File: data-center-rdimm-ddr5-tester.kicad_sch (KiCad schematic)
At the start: 2 parts

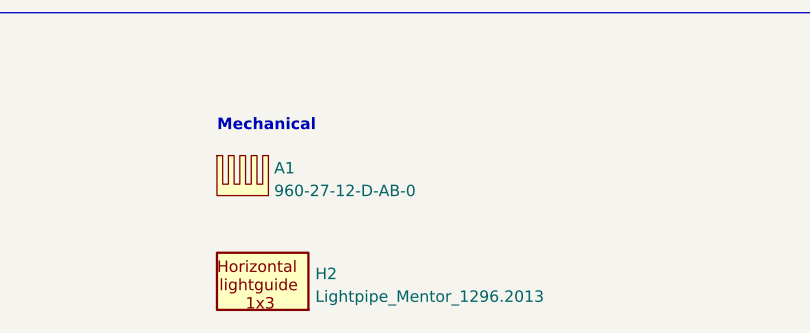
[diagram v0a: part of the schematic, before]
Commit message: [#67402] Connect low speed signals and interfaces to the HD banks. Optimize connection in bank 86
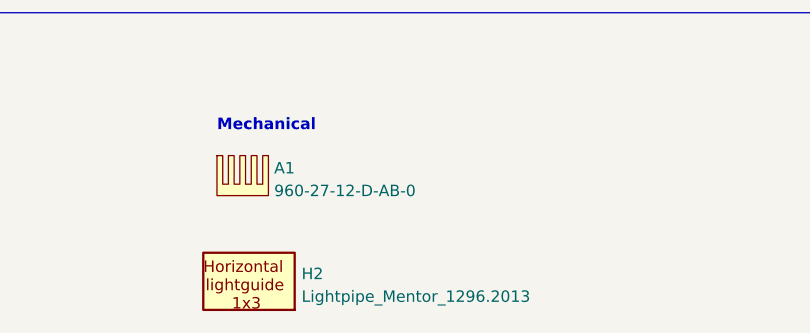
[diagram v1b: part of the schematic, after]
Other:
- moved on the sheet: H2
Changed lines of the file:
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@@
     )
   )
-  (symbol (lib_id "antmicroMechanicalParts:Lightpipe_Mentor_1296.2013") (at 259.08 276.86 0) (unit 1)
+  (symbol (lib_id "antmicroMechanicalParts:Lightpipe_Mentor_1296.2013") (at 257.556 276.86 0) (unit 1)
     (in_bom yes) (on_board yes) (dnp no) (fields_autoplaced)
-    (property "Reference" "H2" (at 264.922 275.3944 0)
+    (property "Reference" "H2" (at 263.398 275.3944 0)
       (effects (font (size 1.27 1.27) (thickness 0.15)) (justify left))
     )
-    (property "Value" "Lightpipe_Mentor_1296.2013" (at 264.922 277.9181 0)
+    (property "Value" "Lightpipe_Mentor_1296.2013" (at 263.398 277.9181 0)
       (effects (font (size 1.27 1.27) (thickness 0.15)) (justify left))
     )
-    (property "Footprint" "antmicro-footprints:Mech_Lightpipe_Mentor_1296.2013" (at 279.4 284.48 0)
+    (property "Footprint" "antmicro-footprints:Mech_Lightpipe_Mentor_1296.2013" (at 277.876 284.48 0)
       (effects (font (size 1.27 1.27) (thickness 0.15)) (justify left bottom) hide)
     )
-    (property "Datasheet" "https://docs.rs-online.com/e47b/0900766b813f6efb.pdf" (at 279.4 287.02 0)
+    (property "Datasheet" "https://docs.rs-online.com/e47b/0900766b813f6efb.pdf" (at 277.876 287.02 0)
       (effects (font (size 1.27 1.27) (thickness 0.15)) (justify left bottom) hide)
     )
-    (property "Manufacturer" "Mentor Worldwide" (at 279.4 289.56 0)
+    (property "Manufacturer" "Mentor Worldwide" (at 277.876 289.56 0)
       (effects (font (size 1.27 1.27) (thickness 0.15)) (justify left bottom) hide)
     )
-    (property "MPN" "1296.2013" (at 279.4 292.1 0)
+    (property "MPN" "1296.2013" (at 277.876 292.1 0)
       (effects (font (size 1.27 1.27) (thickness 0.15)) (justify left bottom) hide)
     )
-    (property "Author" "Antmicro" (at 279.4 294.64 0)
+    (property "Author" "Antmicro" (at 277.876 294.64 0)
       (effects (font (size 1.27 1.27) (thickness 0.15)) (justify left bottom) hide)
     )
-    (property "License" "Apache-2.0" (at 279.4 297.18 0)
+    (property "License" "Apache-2.0" (at 277.876 297.18 0)
       (effects (font (size 1.27 1.27) (thickness 0.15)) (justify left bottom) hide)
     )

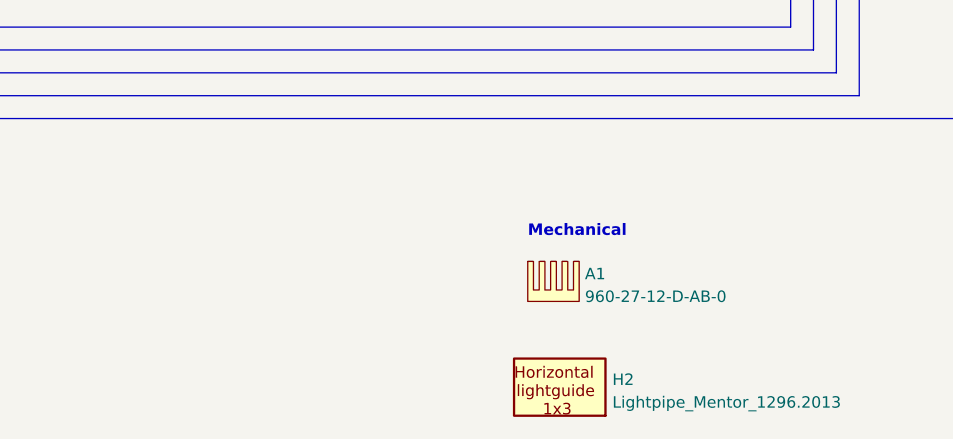
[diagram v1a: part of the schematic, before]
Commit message: [#67402] Add I3C circuit, update I2C DDR
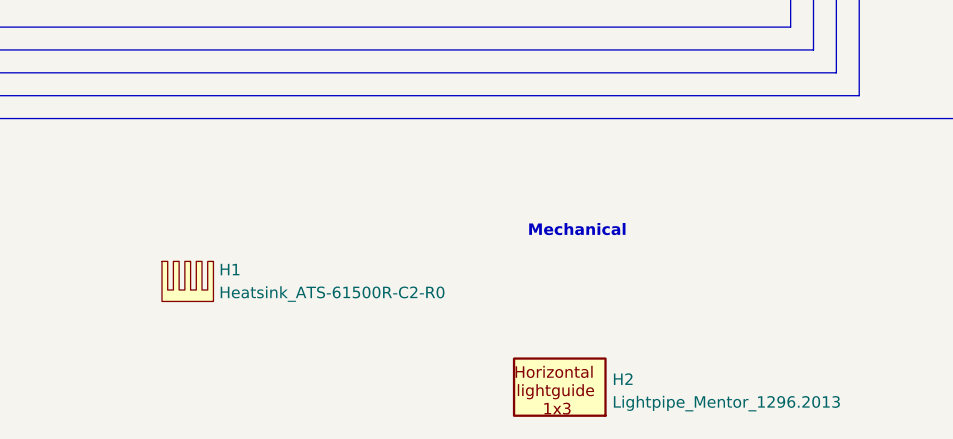
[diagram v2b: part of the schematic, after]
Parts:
- removed A1: Heatsink_960-27-12-D-AB-0, antmicro-footprints:Heatsink_960-27-12-D-AB-0, symbol antmicroMechanicalParts:Heatsink_960-27-12-D-AB-0
- added H1: Heatsink_ATS-61500R-C2-R0, antmicro-footprints:Heatsink_ATS-61500R-C2-R0, symbol antmicroMechanicalParts:Heatsink_ATS-61500R-C2-R0
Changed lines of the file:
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@@
     (effects (font (size 3.9878 3.9878) (thickness 0.7976) bold) (justify left bottom))
   )
-  (symbol (lib_id "antmicroMechanicalParts:Heatsink_960-27-12-D-AB-0") (at 254 262.255 0) (unit 1)
+  (symbol (lib_id "antmicroMechanicalParts:Heatsink_ATS-61500R-C2-R0") (at 213.36 262.255 0) (unit 1)
     (in_bom yes) (on_board yes) (dnp no) (fields_autoplaced)
-    (property "Reference" "A1" (at 260.35 263.6469 0)
+    (property "Reference" "H1" (at 219.71 263.2075 0)
       (effects (font (size 1.27 1.27) (thickness 0.15)) (justify left))
     )
-    (property "Value" "Heatsink_960-27-12-D-AB-0" (at 260.35 266.1706 0)
-      (effects (font (size 1.27 1.27) (thickness 0.15)) (justify left) hide)
+    (property "Value" "Heatsink_ATS-61500R-C2-R0" (at 219.71 265.7475 0)
+      (effects (font (size 1.27 1.27) (thickness 0.15)) (justify left))
     )
-    (property "Footprint" "antmicro-footprints:Heatsink_960-27-12-D-AB-0" (at 271.78 269.875 0)
+    (property "Footprint" "antmicro-footprints:Heatsink_ATS-61500R-C2-R0" (at 231.14 269.875 0)
       (effects (font (size 1.27 1.27) (thickness 0.15)) (justify left bottom) hide)
     )
-    (property "Datasheet" "https://media.digikey.com/pdf/Data%20Sheets/Wakefield%20Thermal%20PDFs/960_Series.pdf" (at 271.78 272.415 0)
+    (property "Datasheet" "https://www.qats.com/DataSheet/ATS-61500-Series-C2-R0" (at 231.14 272.415 0)
       (effects (font (size 1.27 1.27) (thickness 0.15)) (justify left bottom) hide)
     )
-    (property "MPN" "960-27-12-D-AB-0" (at 260.35 266.1706 0)
-      (effects (font (size 1.27 1.27) (thickness 0.15)) (justify left))
-    )
-    (property "Manufacturer" "Wakefield-Vette" (at 271.78 277.495 0)
+    (property "MPN" "ATS-61500R-C2-R0" (at 231.14 274.955 0)
       (effects (font (size 1.27 1.27) (thickness 0.15)) (justify left bottom) hide)
     )
-    (property "Author" "Antmicro" (at 271.78 280.035 0)
+    (property "Manufacturer" "Advanced Thermal Solutions" (at 231.14 277.495 0)
       (effects (font (size 1.27 1.27) (thickness 0.15)) (justify left bottom) hide)
     )
-    (property "License" "Apache-2.0" (at 271.78 282.575 0)
+    (property "Author" "Antmicro" (at 231.14 280.035 0)
+      (effects (font (size 1.27 1.27) (thickness 0.15)) (justify left bottom) hide)
+    )
+    (property "License" "Apache-2.0" (at 231.14 282.575 0)
       (effects (font (size 1.27 1.27) (thickness 0.15)) (justify left bottom) hide)
     )
@@
       (project "data-center-rdimm-ddr5-tester"
         (path "/1faa6543-e26a-4449-8bac-ee14b9f19e5f"
-          (reference "A1") (unit 1)
+          (reference "H1") (unit 1)
         )
       )

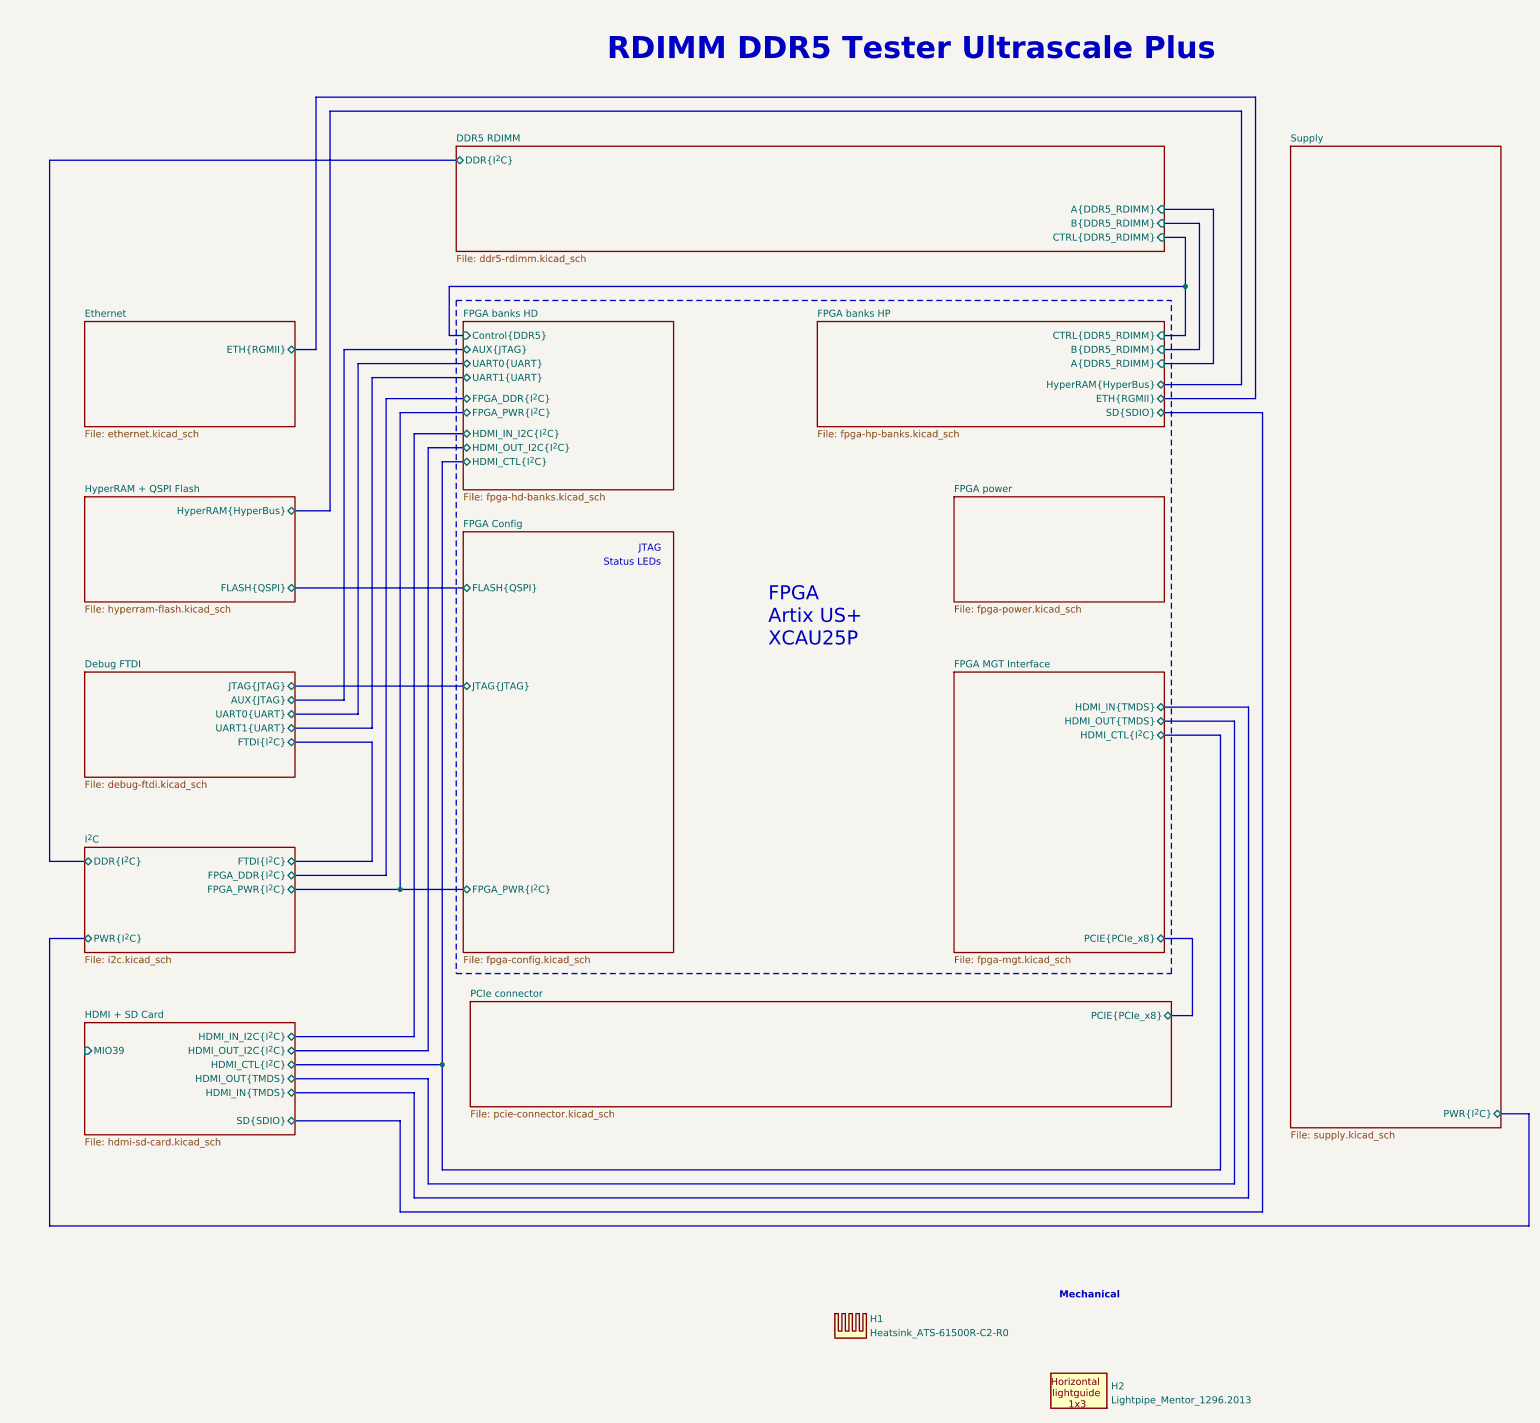
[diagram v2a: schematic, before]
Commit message: [#67725] Connect I3C signals to the FPGA
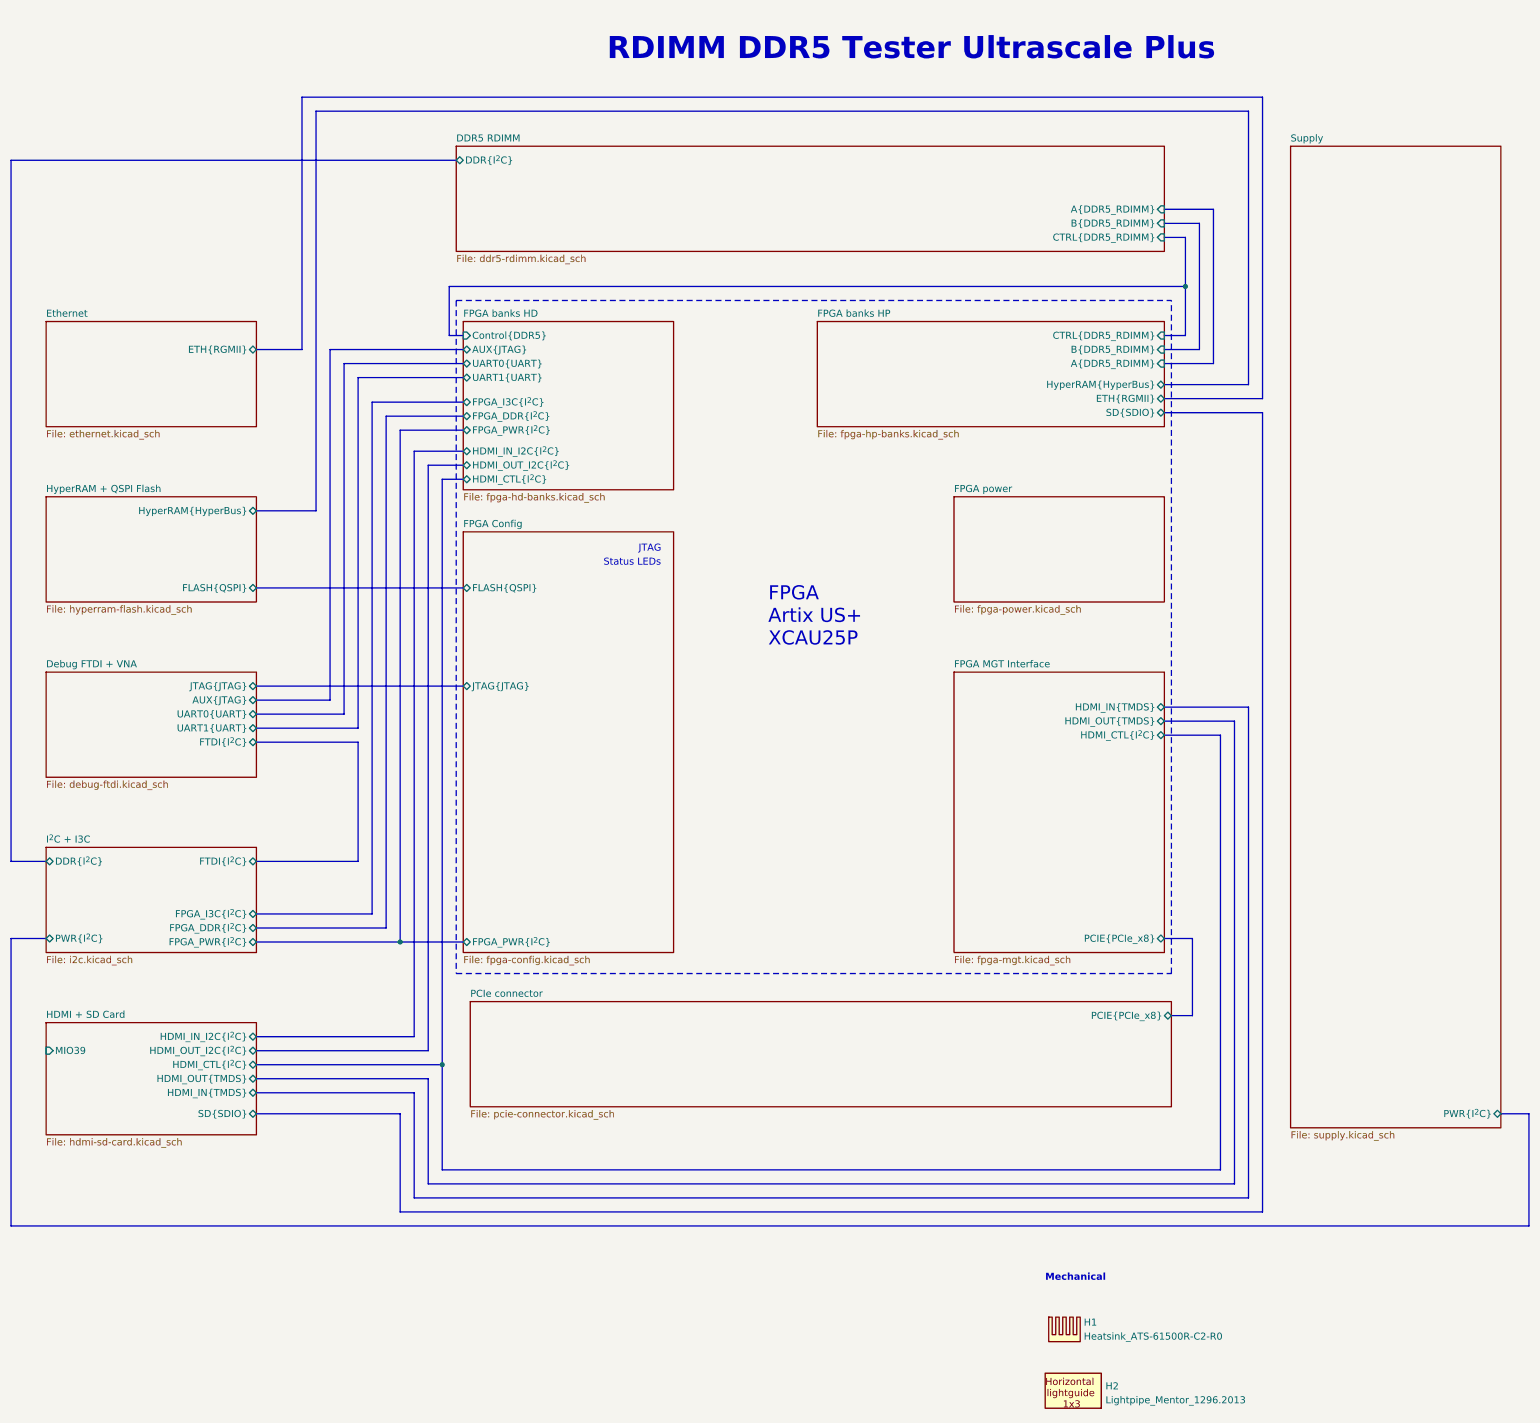
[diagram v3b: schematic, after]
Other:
- sheet Debug FTDI renamed Debug FTDI + VNA
- sheet I^{2}C renamed I^{2}C + I3C
- sheet FPGA banks HD ports: added FPGA_I3C{I^{2}C}; removed none
- sheet I^{2}C + I3C ports: added FPGA_I3C{I^{2}C}; removed none
- moved on the sheet: H1, H2

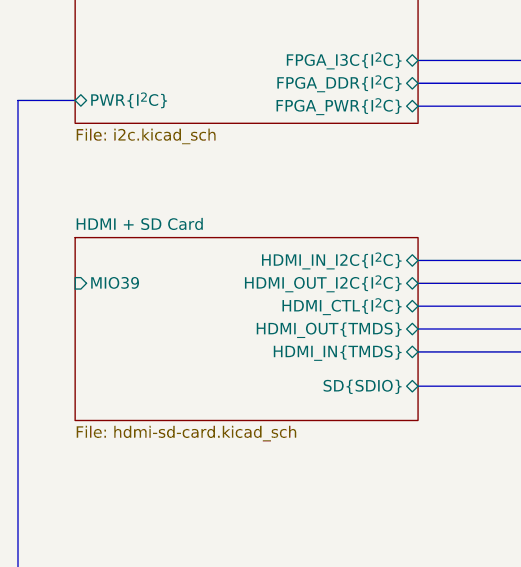
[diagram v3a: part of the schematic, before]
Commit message: [#67725] Import review changes to PCB. Minor schematic fix
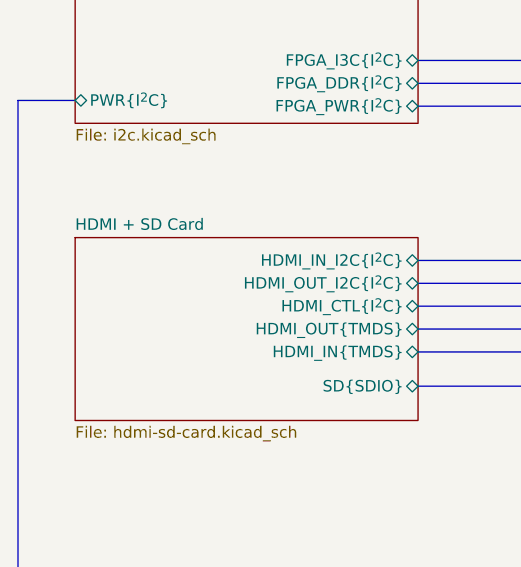
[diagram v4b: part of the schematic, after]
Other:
- sheet HDMI + SD Card ports: added none; removed MIO39
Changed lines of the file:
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@@
       (effects (font (size 1.27 1.27)) (justify right))
-    )
-    (pin "MIO39" input (at 70.485 214.63 180)
-      (effects (font (size 1.27 1.27)) (justify left))
     )
     (pin "HDMI_IN{TMDS}" bidirectional (at 108.585 222.25 0)

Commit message: [#68016] Clean-up the schematic
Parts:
- renumbered H1 to A1
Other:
- note added: "RDIMM DDR5 Tester"
- note removed: "RDIMM DDR5 Tester Ultrascale Plus"
- moved on the sheet: A1, H2
